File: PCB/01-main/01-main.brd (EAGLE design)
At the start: 90 x 46.2 mm, 64 parts, among them CN1 ML8, J1 22057045, J14 22057055, J8 22057045, Q1 C1015, SW1 SK-12D11VG3, T1 BSS138, U1 CH340ESMD, U2 STM32F446RET6, U3 SUNA_LIB_M5STAMP_C3U_MATE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

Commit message: ⚡️基礎配線完了
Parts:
- moved T1 2.83 mm to (-28.0, 51.0), turned to 270 degrees
- moved C14 2.00 mm to (-14.0, 56.5)
- moved C6 2.00 mm to (-23.0, 56.5)
- moved R1 2.00 mm to (-15.5, 59.0)
- moved R2 2.00 mm to (-21.5, 59.0)
- moved U1 2.00 mm to (-18.5, 56.5)
- moved R31 1.12 mm to (-4.00, 46.5)
- moved C1 0.50 mm to (2.50, 60.5)
- moved C16 0.50 mm to (5.00, 48.5)
- moved C2 0.50 mm to (7.50, 53.5)
- moved C3 0.50 mm to (-1.00, 62.0)
- moved C4 0.50 mm to (-1.00, 45.0)
- moved C5 0.50 mm to (-9.50, 53.5)
- moved R30 0.50 mm to (3.00, 46.5)
- moved R4 0.50 mm to (5.50, 57.0)
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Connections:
- removed net N$22: R10.2, U1.6
- removed net N$23: LED18.A, R10.1
- new net N$19: LED18.A, U1.6
- new net N$20: LED18.C, R10.2
- net GND: now also R10.1; no longer J14.3, LED18.C
- net LED-FLOOR: no longer CN1.6
- net MIRROR: no longer CN1.8
- net SIG-FLOOR: no longer CN1.5
- net TOGGLE: now also CN1.8
- net UART3-RX: now also CN1.5
- net UART3-TX: now also CN1.6
- net UART4-TX: now also J14.3
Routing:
- net GND: track 0.00 -> 197.5 mm
- net VDD: track 0.00 -> 73.9 mm
- net +5V: track 0.00 -> 57.4 mm
- net +3V3: track 0.00 -> 52.0 mm
- net UART2-TX: track 0.00 -> 47.2 mm, vias 0 -> 1
- net UART6-RX: track 0.00 -> 46.5 mm, vias 0 -> 1
- net UART2-RX: track 0.00 -> 45.2 mm, vias 0 -> 1
- net UART6-TX: track 0.00 -> 42.7 mm, vias 0 -> 1
- net UART4-TX: track 0.00 -> 33.5 mm, vias 0 -> 1
- net UART4-RX: track 0.00 -> 33.2 mm, vias 0 -> 1
- net SCL: track 0.00 -> 31.7 mm
- net SDA: track 0.00 -> 29.3 mm
- net UART3-TX: track 0.00 -> 24.9 mm, vias 0 -> 1
- net UART3-RX: track 0.00 -> 23.1 mm, vias 0 -> 1
- net UART1-RX: track 0.00 -> 16.5 mm
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
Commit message: ✏️ i2Cのプルアップ抵抗の位置を変更
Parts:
- moved R12 15.7 mm to (31.0, 37.5)
- moved R13 13.0 mm to (31.0, 39.0)
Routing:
- net SDA: track 29.3 -> 36.9 mm
- net SCL: track 31.7 -> 34.0 mm
- net +3V3: track 52.0 -> 53.5 mm
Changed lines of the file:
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@@
 <attribute name="VALUE" x="34.492" y="48.048" size="1.27" layer="27" ratio="10" rot="R270"/>
 </element>
-<element name="R12" library="rcl" library_urn="urn:adsk.eagle:library:334" package="R0402" package3d_urn="urn:adsk.eagle:package:23547/3" value="10k" x="33.5" y="53" smashed="yes">
-<attribute name="POPULARITY" value="0" x="33.5" y="53" size="1.778" layer="27" display="off"/>
-<attribute name="SPICEPREFIX" value="R" x="33.5" y="53" size="1.778" layer="27" display="off"/>
-</element>
-<element name="R13" library="rcl" library_urn="urn:adsk.eagle:library:334" package="R0402" package3d_urn="urn:adsk.eagle:package:23547/3" value="10k" x="36" y="51" smashed="yes">
-<attribute name="POPULARITY" value="0" x="36" y="51" size="1.778" layer="27" display="off"/>
-<attribute name="SPICEPREFIX" value="R" x="36" y="51" size="1.778" layer="27" display="off"/>
+<element name="R12" library="rcl" library_urn="urn:adsk.eagle:library:334" package="R0402" package3d_urn="urn:adsk.eagle:package:23547/3" value="10k" x="31" y="37.5" smashed="yes">
+<attribute name="POPULARITY" value="0" x="31" y="37.5" size="1.778" layer="27" display="off"/>
+<attribute name="SPICEPREFIX" value="R" x="31" y="37.5" size="1.778" layer="27" display="off"/>
+</element>
+<element name="R13" library="rcl" library_urn="urn:adsk.eagle:library:334" package="R0402" package3d_urn="urn:adsk.eagle:package:23547/3" value="10k" x="31" y="39" smashed="yes">
+<attribute name="POPULARITY" value="0" x="31" y="39" size="1.778" layer="27" display="off"/>
+<attribute name="SPICEPREFIX" value="R" x="31" y="39" size="1.778" layer="27" display="off"/>
 </element>
 <element name="U5" library="MAX485" package="SOIC127P600X175-8N" value="MAX485ESA+T" x="-11.5" y="43" smashed="yes" rot="R180">
@@
 <wire x1="-1.85" y1="62" x2="-2.3739" y2="62" width="0.254" layer="1"/>
 <wire x1="-2.3739" y1="62" x2="-3.57905" y2="60.79485" width="0.254" layer="1"/>
-<wire x1="33" y1="53" x2="35.5" y2="51" width="0" layer="19" extent="1-1"/>
-<wire x1="31.19" y1="48.81" x2="33" y2="53" width="0" layer="19" extent="1-1"/>
+<wire x1="30.5" y1="37.5" x2="30.5" y2="39" width="0.254" layer="1"/>
+<wire x1="30.5" y1="39" x2="31.19" y2="48.81" width="0" layer="19" extent="1-1"/>
 <wire x1="7.5" y1="54.35" x2="31.19" y2="48.81" width="0" layer="19" extent="1-1"/>
 <wire x1="5.853553125" y1="56.64644375" x2="5.7175125" y2="54.9142125" width="0" layer="19" extent="1-1"/>
@@
 <contactref element="U2" pad="62"/>
 <contactref element="R12" pad="2"/>
-<wire x1="31.19" y1="43.73" x2="29.92" y2="45" width="0.254" layer="1"/>
+<wire x1="31.19" y1="43.73" x2="30.96" y2="43.96" width="0.254" layer="1"/>
+<wire x1="30.96" y1="43.96" x2="29.92" y2="45" width="0.254" layer="1"/>
 <wire x1="8.855084375" y1="47.534" x2="5.01040625" y2="51.378678125" width="0.254" layer="1"/>
 <wire x1="10.31800625" y1="47.534" x2="8.855084375" y2="47.534" width="0.254" layer="1"/>
 <wire x1="12.85200625" y1="45" x2="10.31800625" y2="47.534" width="0.254" layer="1"/>
 <wire x1="29.92" y1="45" x2="12.85200625" y2="45" width="0.254" layer="1"/>
-<wire x1="31.19" y1="43.73" x2="34" y2="53" width="0" layer="19" extent="1-1"/>
+<wire x1="31.5" y1="37.5" x2="31.5" y2="37.9907875" width="0.254" layer="1"/>
+<wire x1="32.9070375" y1="42.0129625" x2="31.19" y2="43.73" width="0.254" layer="1"/>
+<wire x1="31.5" y1="37.9907875" x2="32.9070375" y2="39.397825" width="0.254" layer="1"/>
+<wire x1="32.9070375" y1="39.397825" x2="32.9070375" y2="42.0129625" width="0.254" layer="1"/>
 </signal>
 <signal name="SCL">
@@
 <wire x1="29.694" y1="42.686" x2="31.19" y2="41.19" width="0.254" layer="1"/>
 <wire x1="12.62600625" y1="42.686" x2="29.694" y2="42.686" width="0.254" layer="1"/>
-<wire x1="31.19" y1="41.19" x2="36.5" y2="51" width="0" layer="19" extent="1-1"/>
+<wire x1="31.5" y1="39" x2="31.19" y2="39.31" width="0.254" layer="1"/>
+<wire x1="31.19" y1="39.31" x2="31.19" y2="41.19" width="0.254" layer="1"/>
 </signal>
 <signal name="UART2-TX">

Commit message: ⚡️ ERC
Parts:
- added J2, J3: 22057025, con-molex-5268:CON_22057025_MOL
- moved J14 1.00 mm to (15.0, 30.5)
- moved C1 0.71 mm to (3.00, 61.0)
- moved R31 0.50 mm to (-4.00, 46.0)
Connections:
- removed net LED-FLOOR: U2.36
- removed net LED-UI: U2.35
- removed net MIRROR: U2.44
- removed net SIG-FLOOR: U2.8
- removed net SWCLK: U2.49
- removed net SWDIO: U2.46
- new net CAM-LED-L: J3.2, U2.36
- new net CAM-LED-R: J2.2, U2.35
- net GND: now also J2.1, J3.1
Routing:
- net VDD: track 73.9 -> 72.9 mm

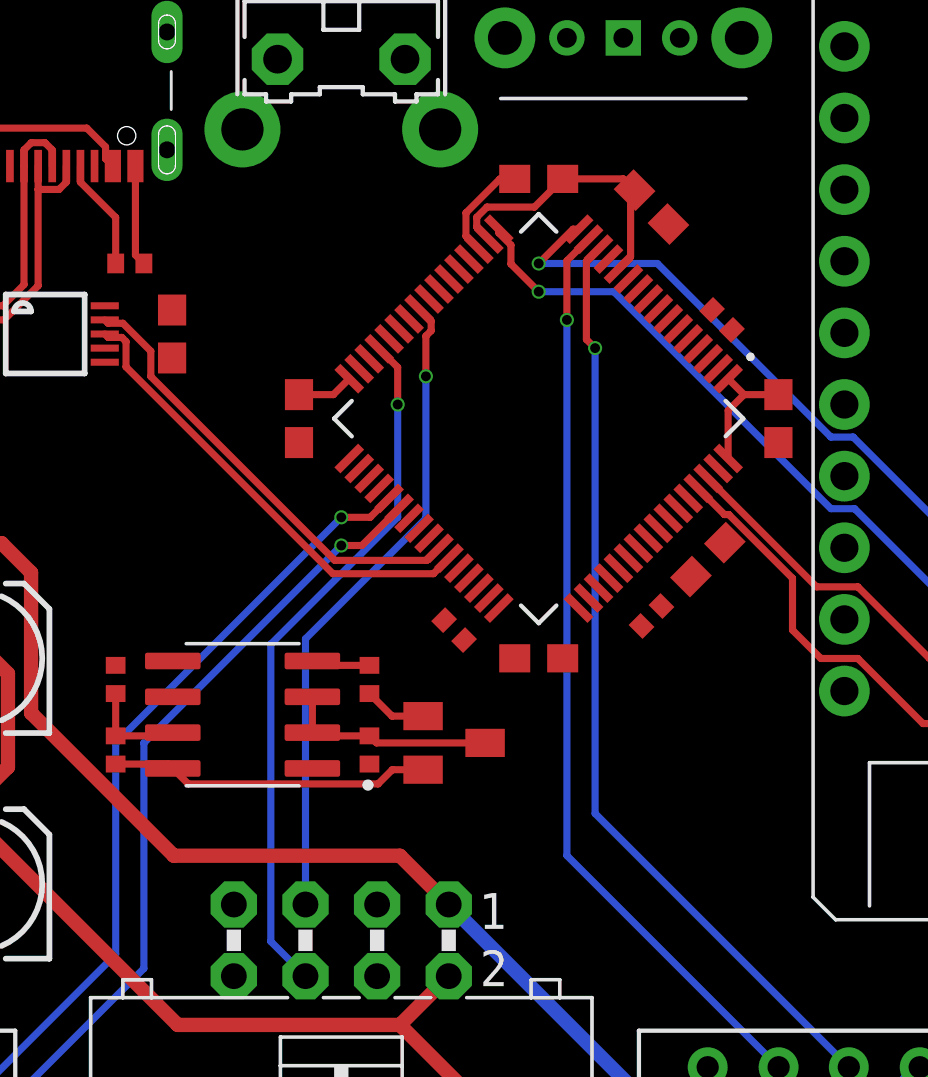
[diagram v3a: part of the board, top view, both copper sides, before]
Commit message: ⚡️ パスコンの位置を調整
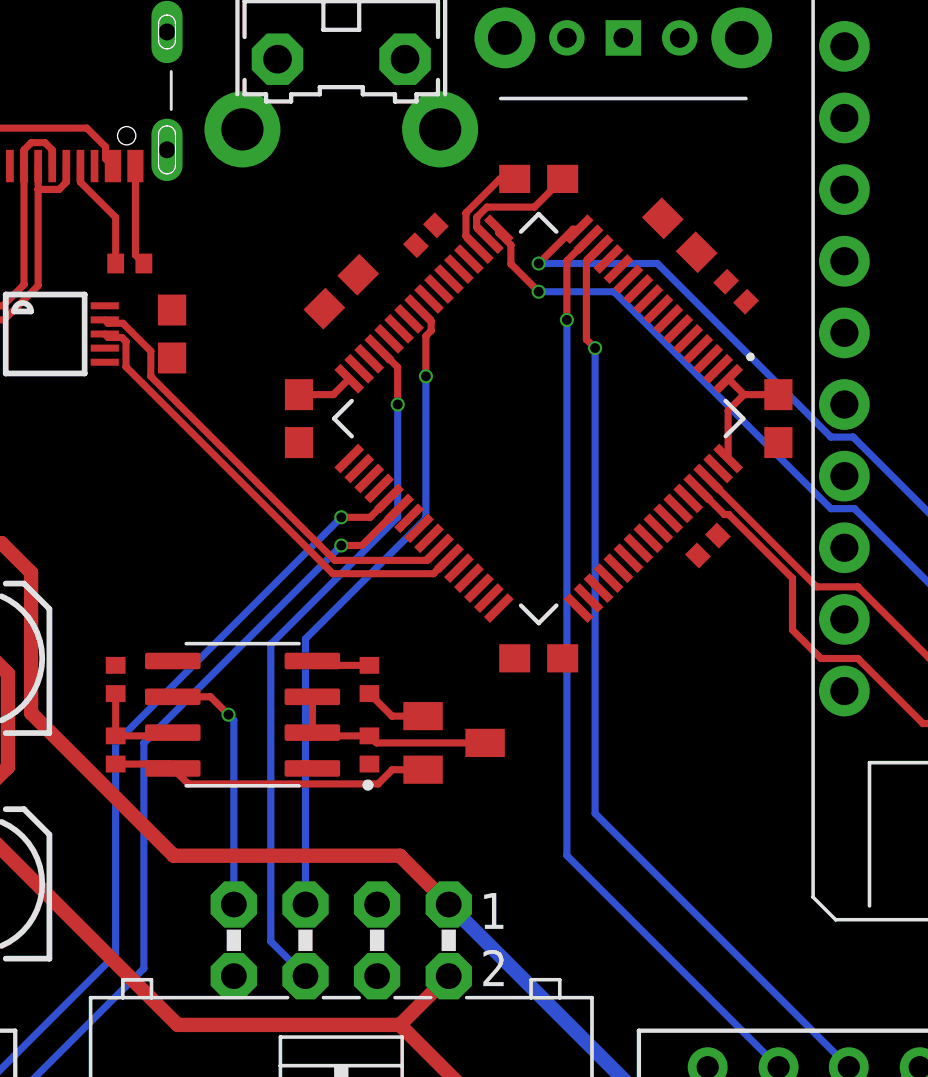
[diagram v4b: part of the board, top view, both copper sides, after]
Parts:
- moved R30 11.9 mm to (6.00, 58.0), turned to 135 degrees
- moved C16 11.5 mm to (4.00, 60.0), turned to 135 degrees
- moved C1 11.4 mm to (-8.00, 58.0), turned to 225 degrees
- moved R4 10.9 mm to (-5.00, 60.0), turned to 225 degrees
- moved R31 9.49 mm to (5.00, 49.0), turned to 225 degrees
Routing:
- net SERVO-SIG: track 0.00 -> 9.05 mm, vias 0 -> 1
- net GND: track 197.2 -> 191.4 mm

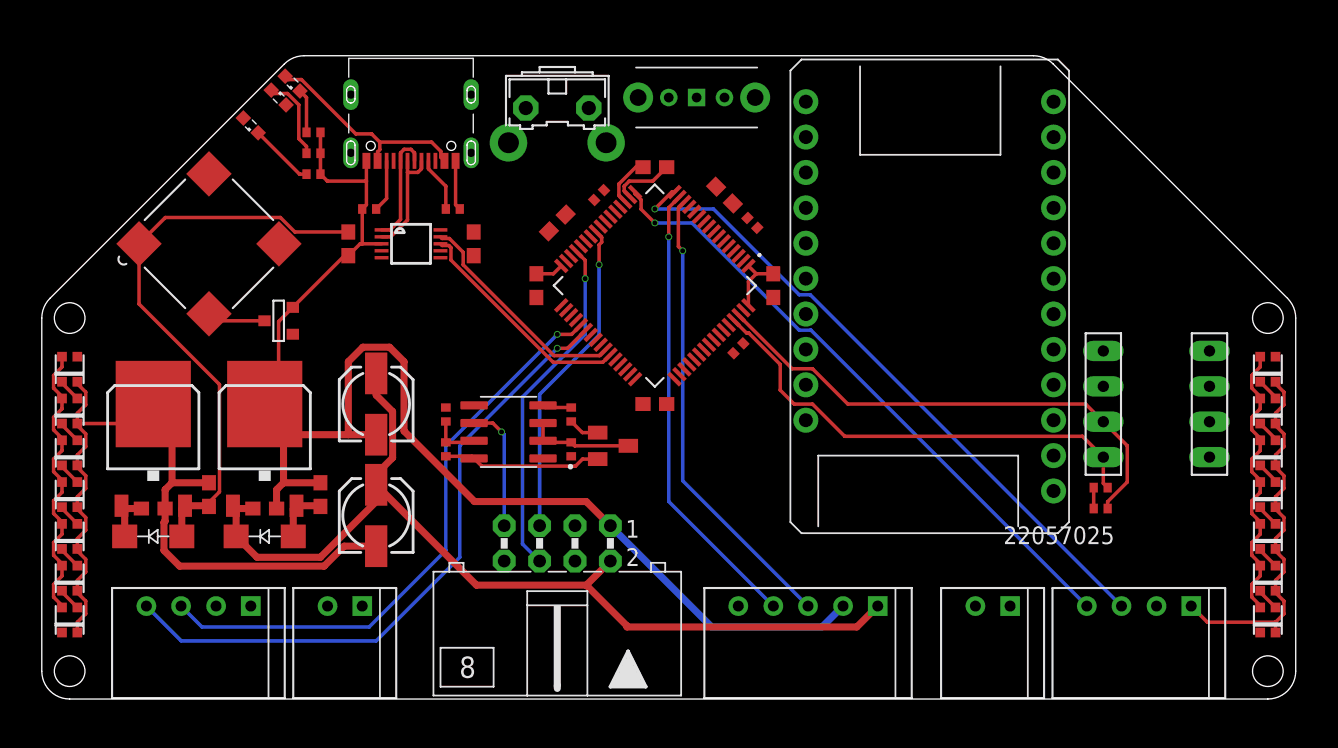
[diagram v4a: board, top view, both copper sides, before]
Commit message: ⚡️ 10milに改良
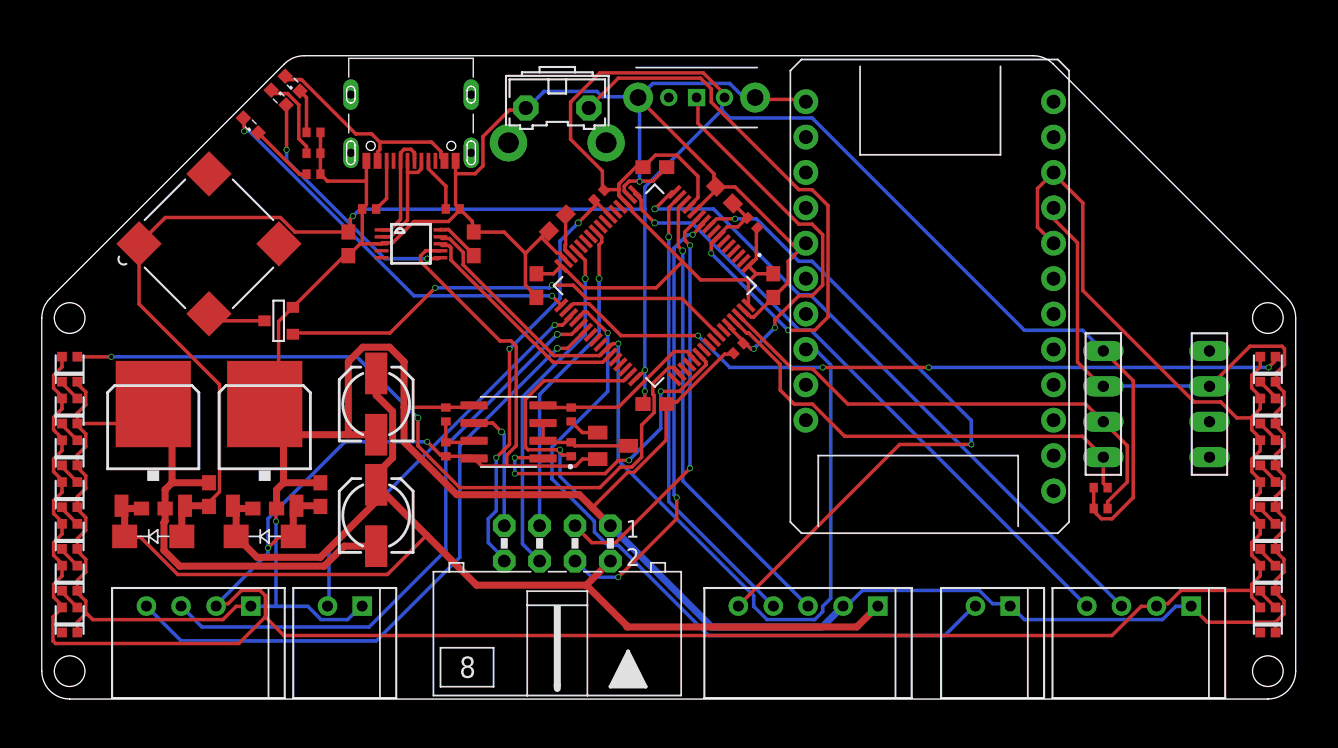
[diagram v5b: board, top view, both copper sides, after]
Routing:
- net GND: track 191.4 -> 411.4 mm, vias 0 -> 3
- net +5V: track 57.4 -> 231.7 mm, vias 0 -> 2
- net +3V3: track 53.5 -> 204.3 mm, vias 0 -> 3
- net LED-L: track 0.00 -> 54.8 mm, vias 0 -> 2
- net LED-R: track 0.00 -> 53.5 mm, vias 0 -> 4
- net CAM-LED-L: track 0.00 -> 51.7 mm, vias 0 -> 1
- net UART1-TX: track 16.1 -> 65.9 mm, vias 0 -> 1
- net LED-TOP: track 0.00 -> 48.3 mm, vias 0 -> 2
- net NRST: track 0.00 -> 47.1 mm, vias 0 -> 2
- net SPK: track 0.00 -> 33.5 mm, vias 0 -> 2
- net LOADCELL-L: track 0.00 -> 32.0 mm, vias 0 -> 3
- net TOGGLE: track 0.00 -> 31.1 mm, vias 0 -> 3
- net LOADCELL-R: track 0.00 -> 29.6 mm, vias 0 -> 2
- net LED-WHITE: track 0.00 -> 28.9 mm, vias 0 -> 2
- net CAM-LED-R: track 0.00 -> 28.4 mm, vias 0 -> 1
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
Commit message: ✨ ビアうち完了
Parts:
- moved C13 1.00 mm to (-21.0, 46.0)
- moved C9 1.00 mm to (-21.0, 38.0)
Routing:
- net GND: track 411.4 -> 402.8 mm, vias 3 -> 52
- net +5V: track 231.7 -> 226.6 mm
- net LED-TOP: track 48.3 -> 51.3 mm
- net VDD: track 96.8 -> 98.4 mm
- net +3V3: track 204.3 -> 203.2 mm
- added copper zone on layer 1, net GND
- added copper zone on layer 16, net GND

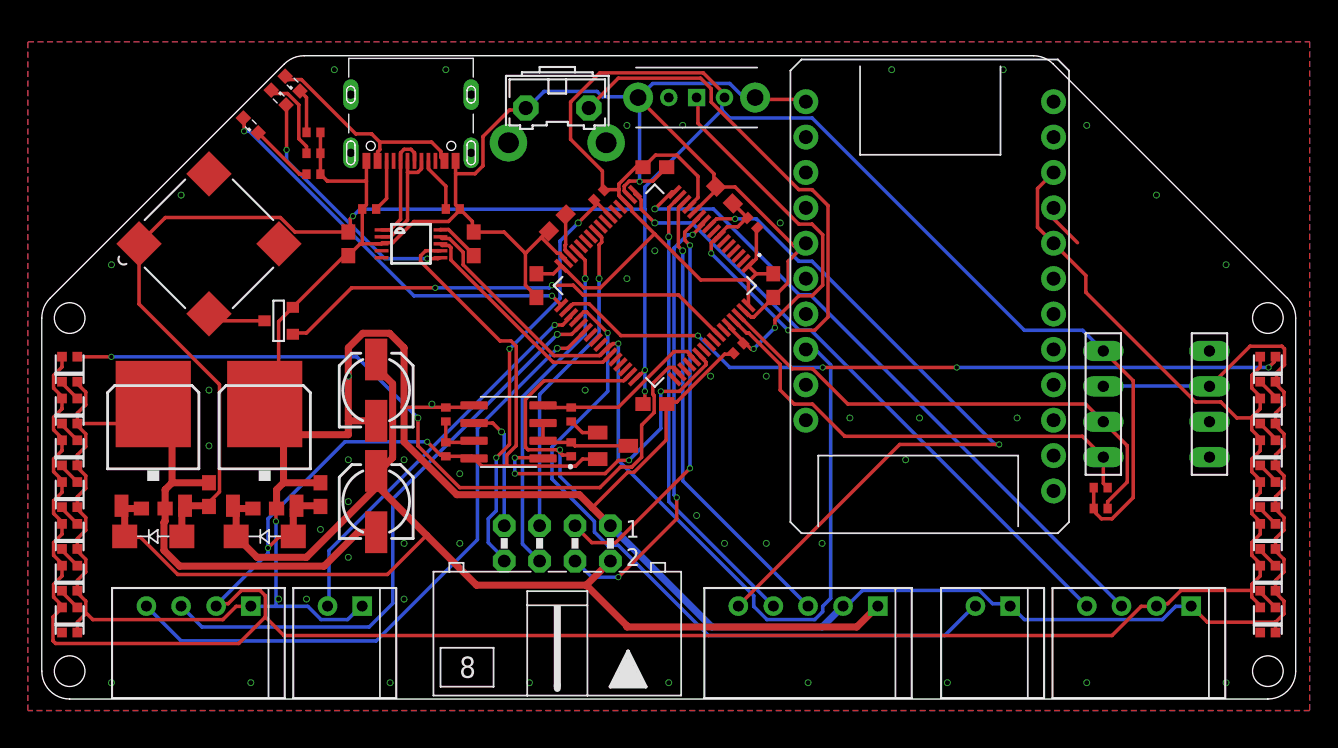
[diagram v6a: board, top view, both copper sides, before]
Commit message: ✨ シルク完了
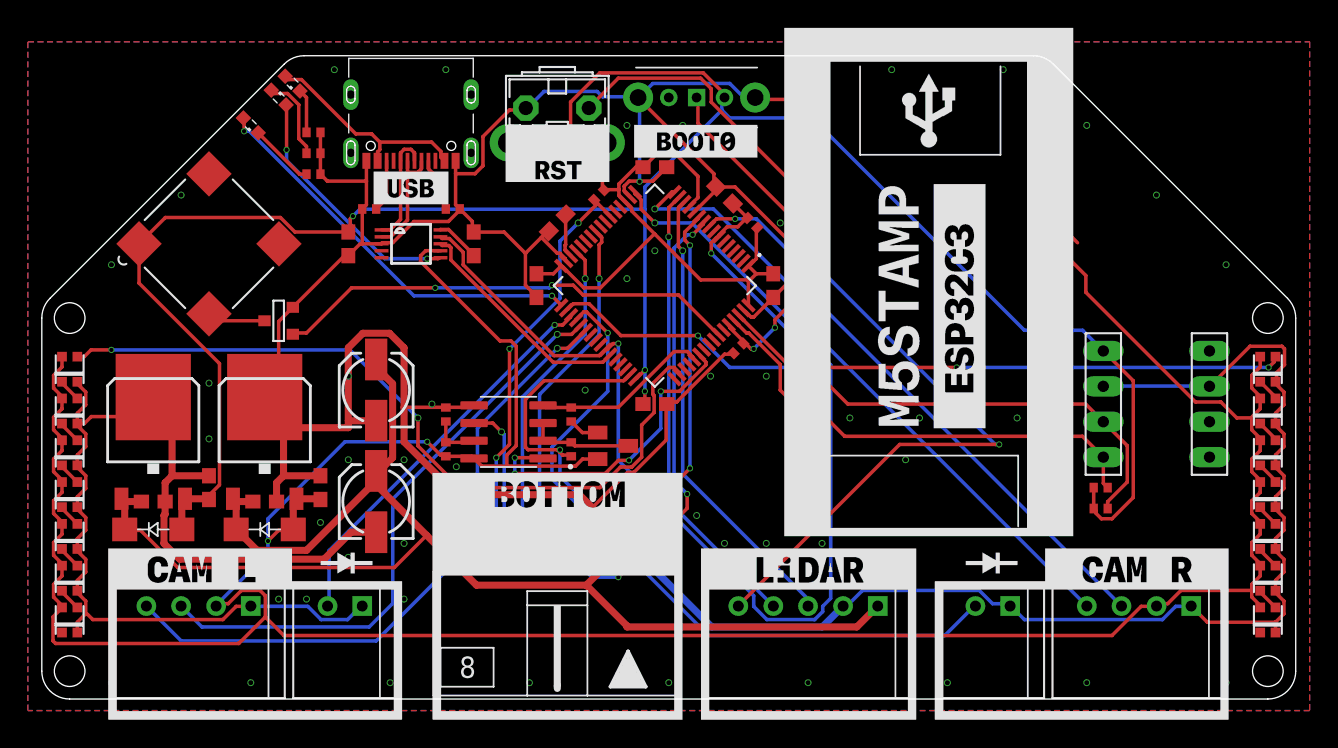
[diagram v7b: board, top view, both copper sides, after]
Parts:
- moved C11 0.50 mm to (-25.0, 39.0)
- moved C17 0.50 mm to (-37.0, 38.0)
- moved C7 0.50 mm to (-33.0, 39.0)
- moved C8 0.50 mm to (-29.0, 38.0)
- moved D1 0.50 mm to (-37.0, 36.0)
- moved D2 0.50 mm to (-29.0, 36.0)
- moved REG1 0.50 mm to (-37.0, 43.0)
- moved REG2 0.50 mm to (-29.0, 43.0)
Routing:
- net GND: track 402.8 -> 394.9 mm, vias 52 -> 49
- net VDD: track 98.4 -> 97.7 mm
- net LOADCELL-L: track 32.0 -> 32.6 mm
- net +3V3: track 203.2 -> 202.7 mm
